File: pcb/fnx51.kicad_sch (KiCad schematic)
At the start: 50 parts, among them J1 Screw_Terminal_01x10, J2 SPI0, J3 SPI1, J4 ATX-24, Q1 BC557, Q2 BC557, Q3 BC547, SW1 POWER, SW2 RESET, U1 74HCT125, U10 AS6C4008-55PCN, U11 74HC04, U2 74HC139, U3 4053, U4 4053, U5 NE555P, U6 74HC00, U7 AT89C51ED2-SMSUM, U8 74HC573, U9 74HC157, Y1 20MHz

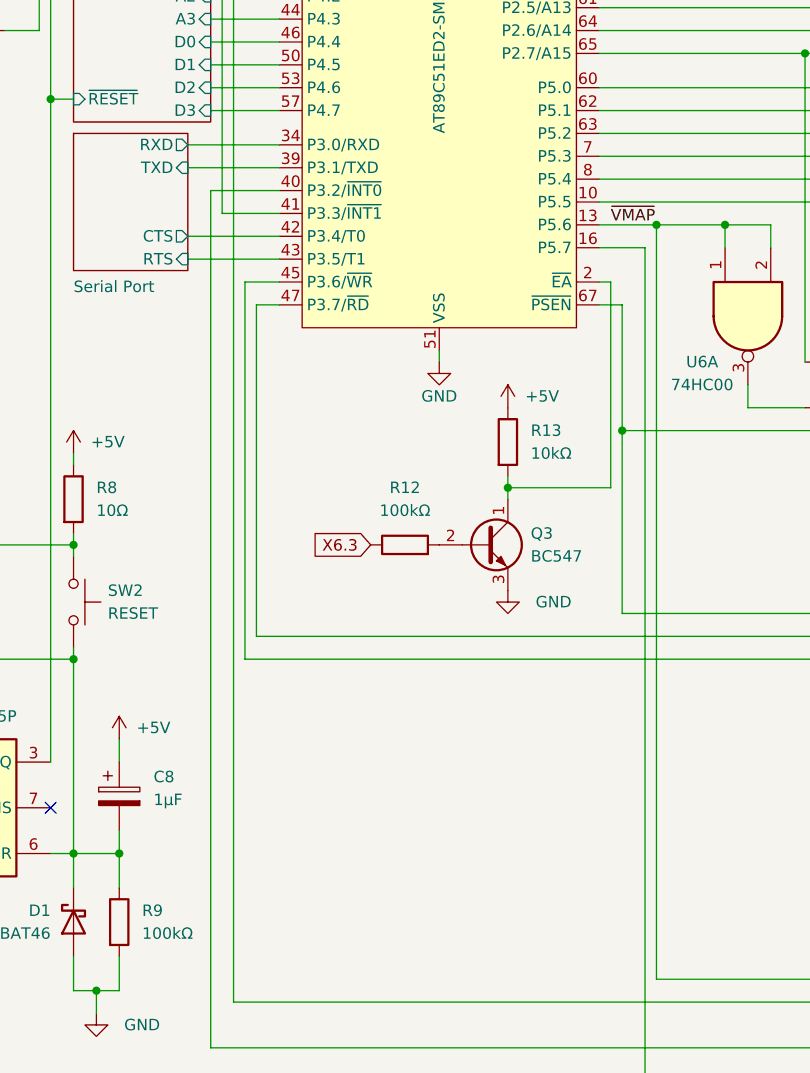
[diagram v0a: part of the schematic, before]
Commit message: update to kicad 10 and fix vertical video timing
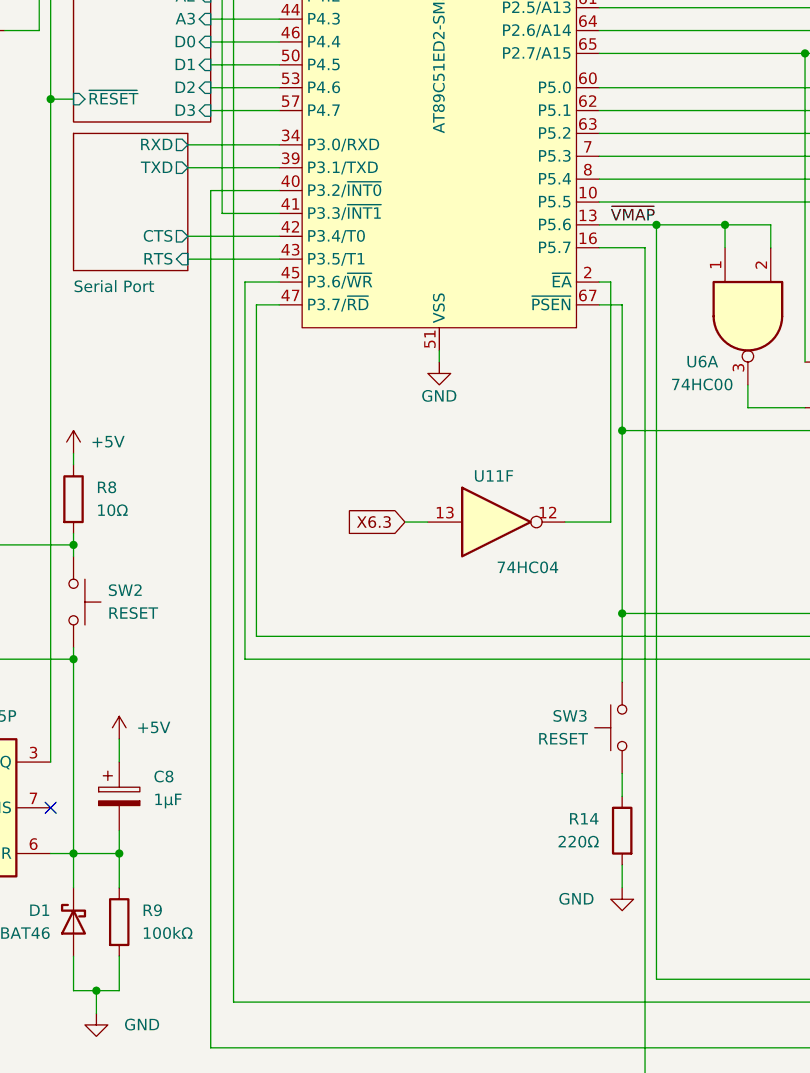
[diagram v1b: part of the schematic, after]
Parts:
- removed Q3: BC547, Package_TO_SOT_THT:TO-92_Inline, symbol Transistor_BJT:BC547
- removed R12: 100kΩ, symbol Device:R
- removed R13: 10kΩ, symbol Device:R
- added R14: 220Ω, symbol Device:R
- added SW3: RESET, symbol Switch:SW_Push
- added unit 6 of U11
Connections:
- net GND: now also R14.2
- net X6.3: now also U11.13
- net ~{PSEN}: now also SW3.1
- net at U7.2 (~{EA}): now also U11.12
- new net: R14.1, SW3.2
